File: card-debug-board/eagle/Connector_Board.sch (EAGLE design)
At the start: 26 parts, among them J1 ORESAT-DEBUG-CONNECTOR-CARD, J3 USB_A_SMT_FEMALE, U1 FT230XS-R

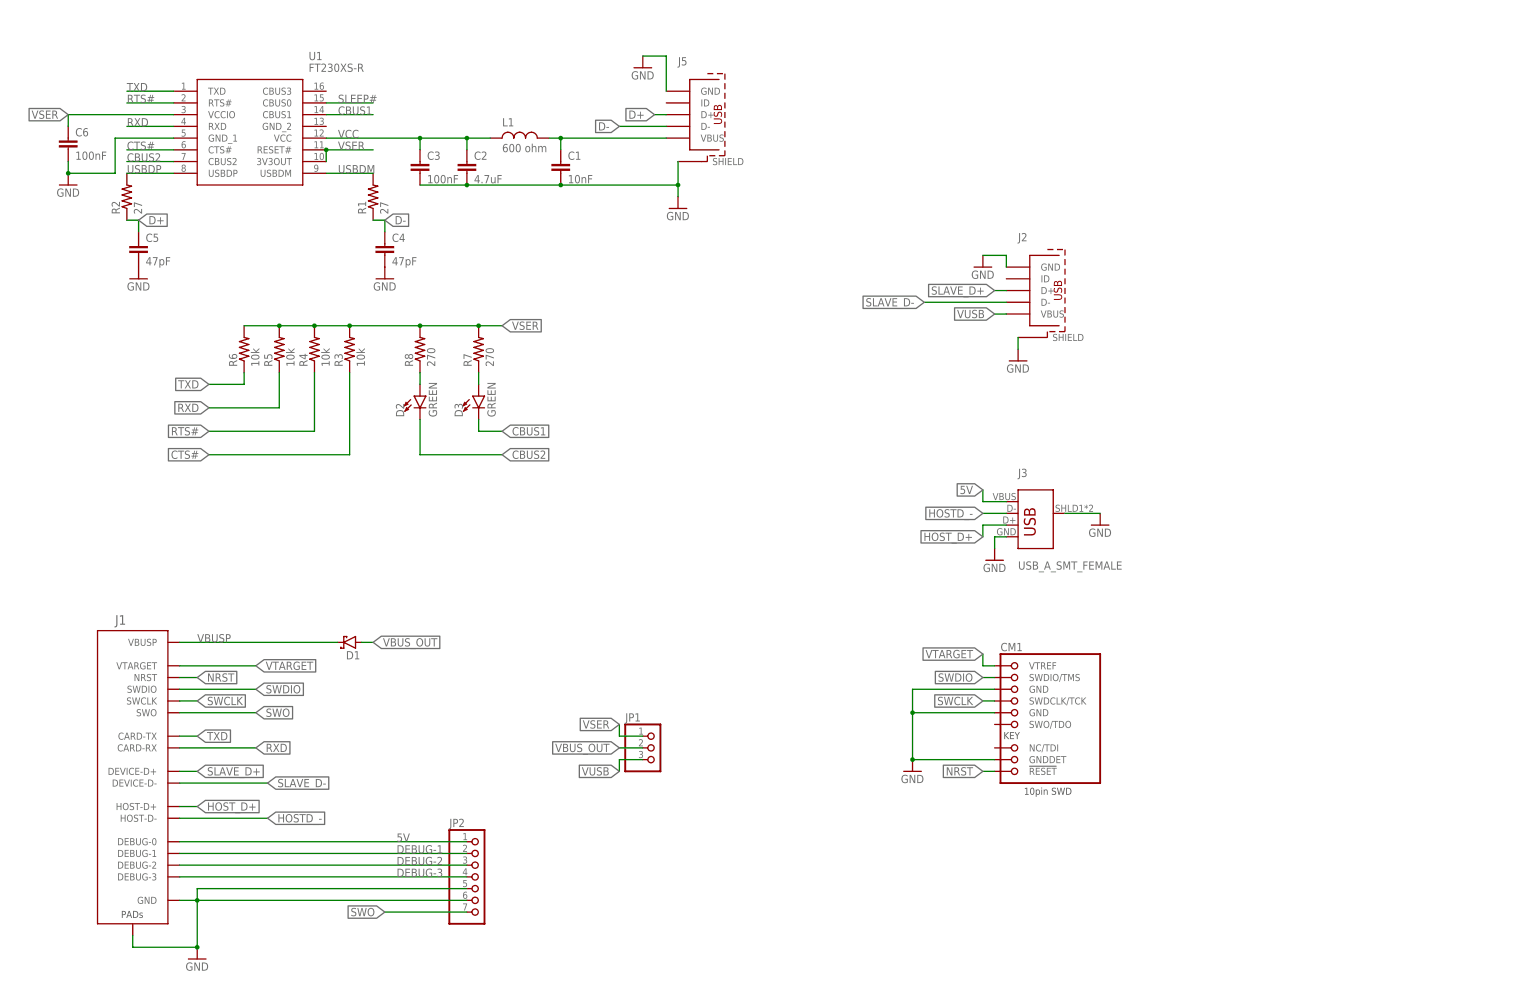
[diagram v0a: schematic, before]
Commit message: Added lables, diff pairs , GND vias
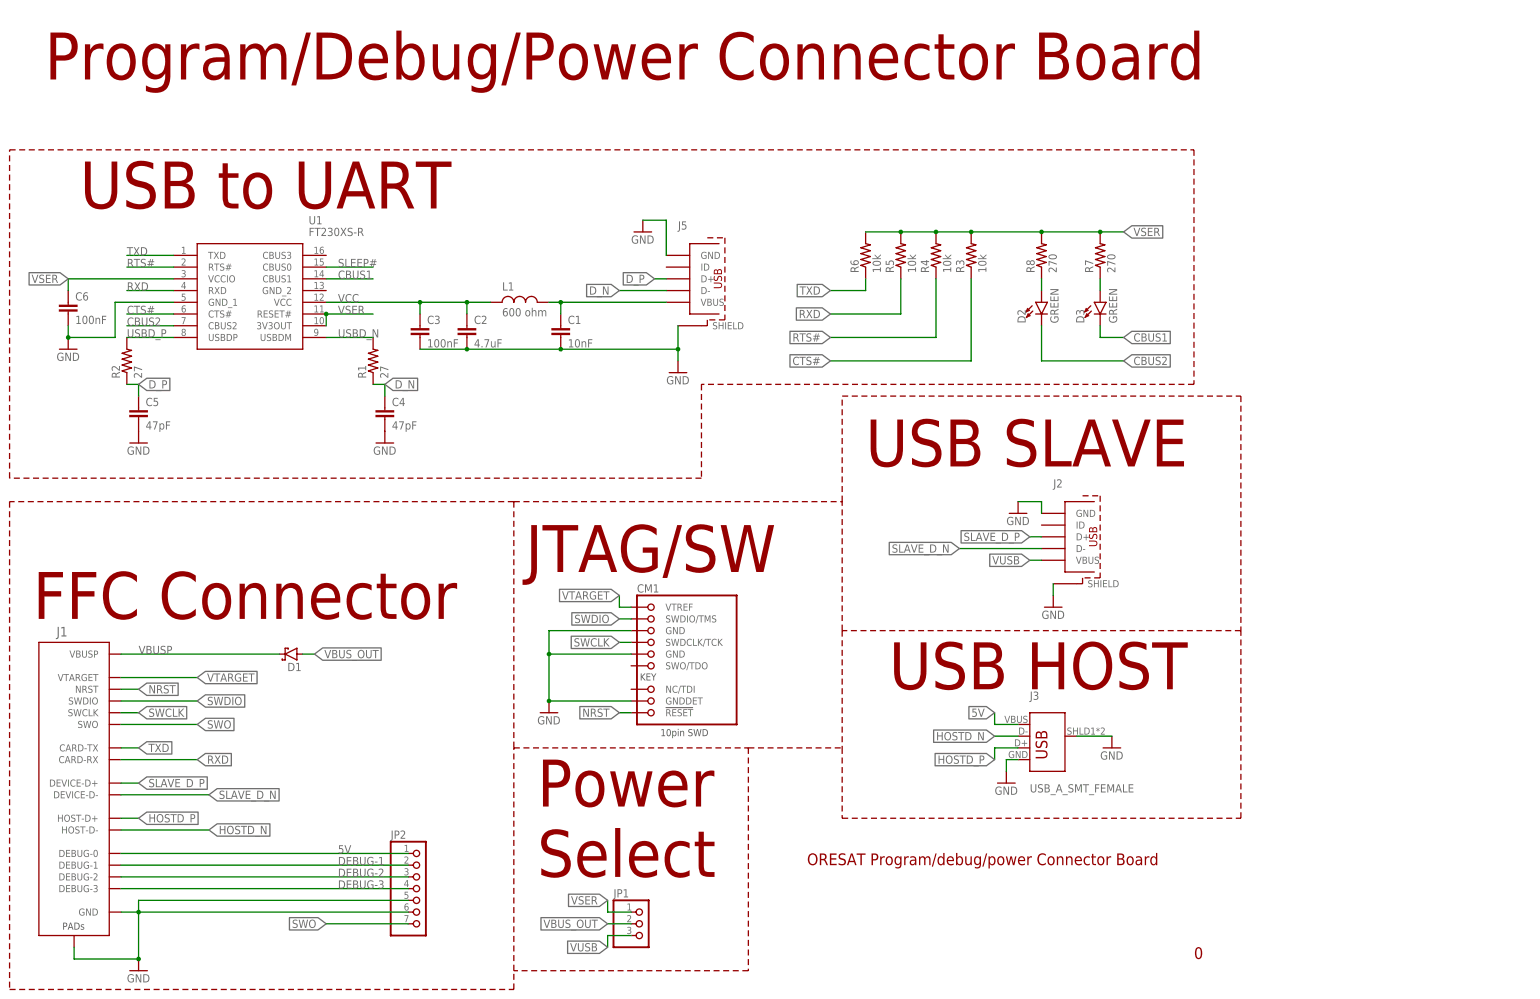
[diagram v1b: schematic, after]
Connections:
- net D+ renamed D_P
- net D- renamed D_N
- net HOSTD_- renamed HOSTD_N
- net HOST_D+ renamed HOSTD_P
- net SLAVE_D+ renamed SLAVE_D_P
- net SLAVE_D- renamed SLAVE_D_N
- net USBDM renamed USBD_N
- net USBDP renamed USBD_P
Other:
- note added: "0"
- note added: "FFC Connector"
- note added: "JTAG/SW"
- note added: "ORESAT Program/debug/power Connector Board"
- note added: "Power Select"
- note added: "Program/Debug/Power Connector Board"
- note added: "USB HOST"
- note added: "USB SLAVE"
- note added: "USB to UART"
- moved on the sheet: C1, C2, C3, C4, C5, C6, CM1, D1, D2, D3, J1, J2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

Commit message: Added P Channel  MOSFET switched VUSB
Made Voltage buses wider
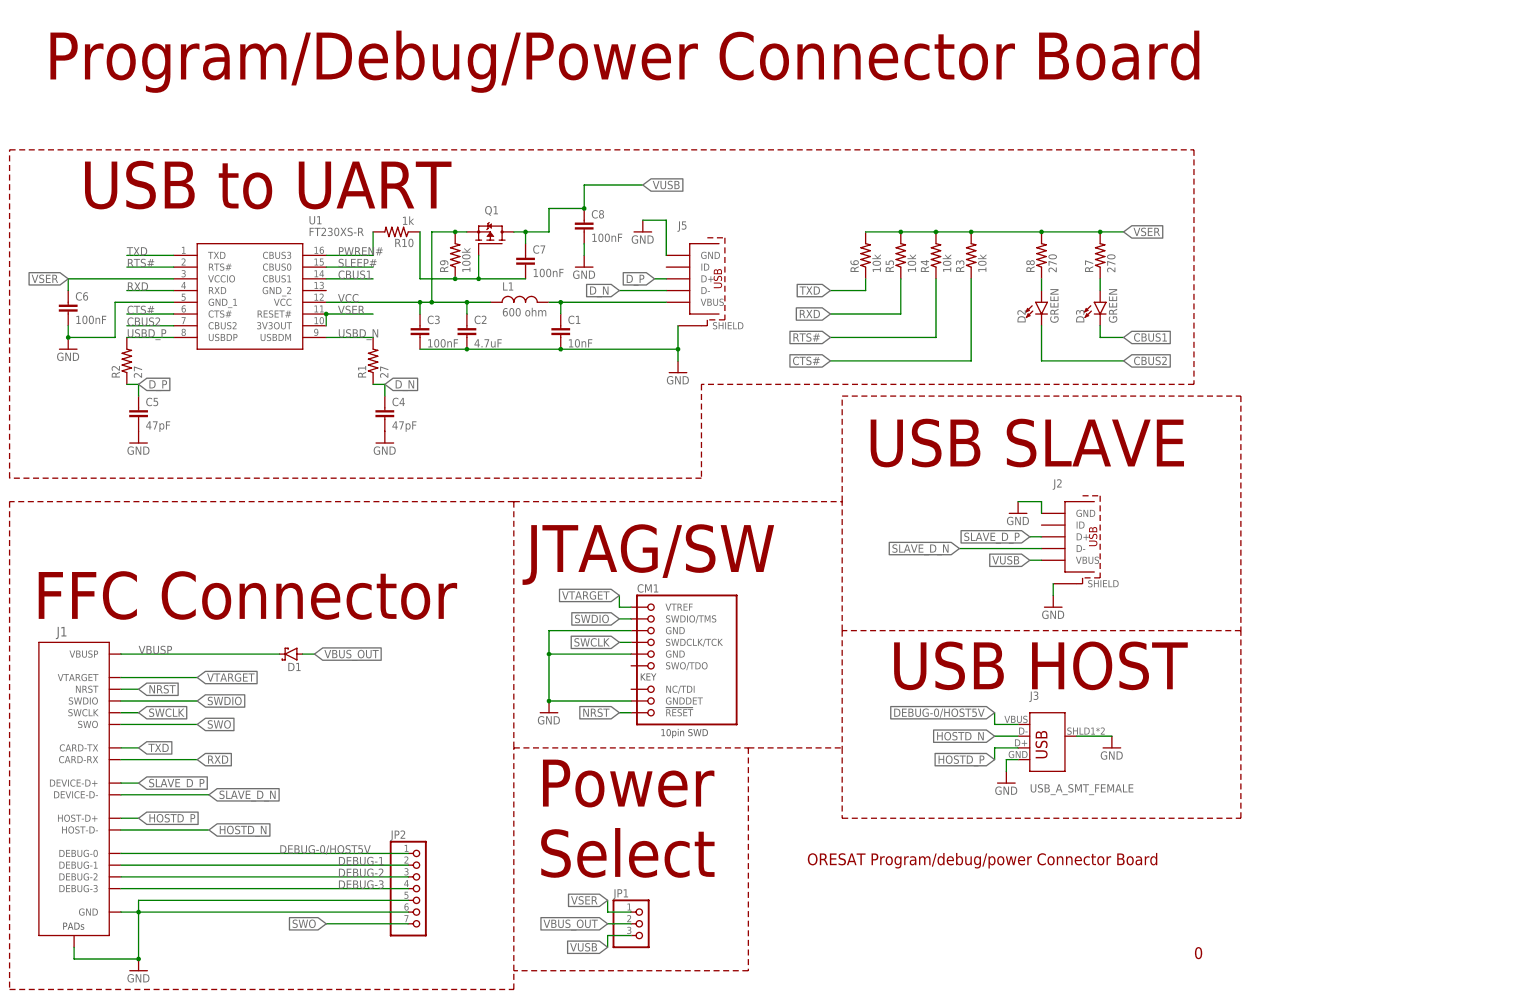
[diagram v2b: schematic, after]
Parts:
- added C7, C8: 100nF, oresat-rcl:C-EU0603-C-NOSILK
- added Q1: MOSFET-PCH-SOT23-6, Q-MOSFET-PCH-SOT23-6:MOSFET-PCH-SOT23-6
- added R10: 1k, oresat-rcl:R-US_0603-C-NOSILK
- added R9: 100k, oresat-rcl:R-US_0603-C-NOSILK
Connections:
- net 5V renamed DEBUG-0/HOST5V
- new net N$3: C7.2, Q1.G, R10.1, R9.1
- new net PWREN#: R10.2, U1.CBUS3
- net GND: now also C8.2
- net VCC: now also Q1.S, R9.2
- net VUSB: now also C7.1, C8.1, Q1.D
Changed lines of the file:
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@@
 <part name="D2" library="SparkFun-LED" library_urn="urn:adsk.eagle:library:529" deviceset="LED-GREEN" device="0603" package3d_urn="urn:adsk.eagle:package:39354/1" value="GREEN"/>
 <part name="D3" library="SparkFun-LED" library_urn="urn:adsk.eagle:library:529" deviceset="LED-GREEN" device="0603" package3d_urn="urn:adsk.eagle:package:39354/1" value="GREEN"/>
+<part name="Q1" library="Q-MOSFET-PCH-SOT23-6" deviceset="MOSFET-PCH-SOT23-6" device=""/>
+<part name="R9" library="oresat-rcl" deviceset="R-US_" device="0603-C-NOSILK" value="100k"/>
+<part name="R10" library="oresat-rcl" deviceset="R-US_" device="0603-C-NOSILK" value="1k"/>
+<part name="C7" library="oresat-rcl" deviceset="C-EU" device="0603-C-NOSILK" value="100nF"/>
+<part name="C8" library="oresat-rcl" deviceset="C-EU" device="0603-C-NOSILK" value="100nF"/>
+<part name="GND12" library="supply1" library_urn="urn:adsk.eagle:library:371" deviceset="GND" device=""/>
 </parts>
 <sheets>
@@
 <attribute name="VALUE" x="245.745" y="145.288" size="1.778" layer="96" font="vector" rot="R90" align="top-left"/>
 </instance>
+<instance part="Q1" gate="G$1" x="111.76" y="162.56" smashed="yes" rot="R90">
+<attribute name="NAME" x="110.49" y="168.91" size="1.778" layer="95"/>
+</instance>
+<instance part="R9" gate="R" x="104.14" y="160.02" smashed="yes" rot="R90">
+<attribute name="NAME" x="102.6414" y="156.21" size="1.778" layer="95" rot="R90"/>
+<attribute name="VALUE" x="107.442" y="156.21" size="1.778" layer="96" rot="R90"/>
+</instance>
+<instance part="R10" gate="R" x="91.44" y="165.1" smashed="yes" rot="R180">
+<attribute name="NAME" x="95.25" y="163.6014" size="1.778" layer="95" rot="R180"/>
+<attribute name="VALUE" x="95.25" y="168.402" size="1.778" layer="96" rot="R180"/>
+</instance>
+<instance part="C7" gate="CE" x="119.38" y="160.02" smashed="yes">
+<attribute name="NAME" x="120.904" y="160.401" size="1.778" layer="95"/>
+<attribute name="VALUE" x="120.904" y="155.321" size="1.778" layer="96"/>
+</instance>
+<instance part="C8" gate="CE" x="132.08" y="167.64" smashed="yes">
+<attribute name="NAME" x="133.604" y="168.021" size="1.778" layer="95"/>
+<attribute name="VALUE" x="133.604" y="162.941" size="1.778" layer="96"/>
+</instance>
+<instance part="GND12" gate="1" x="132.08" y="157.48" smashed="yes">
+<attribute name="VALUE" x="129.54" y="154.94" size="1.778" layer="96"/>
+</instance>
 </instances>
 <busses>
@@
 <wire x1="30.48" y1="142.24" x2="20.32" y2="142.24" width="0.1524" layer="91"/>
 </segment>
+<segment>
+<pinref part="C8" gate="CE" pin="2"/>
+<pinref part="GND12" gate="1" pin="GND"/>
+<wire x1="132.08" y1="162.56" x2="132.08" y2="160.02" width="0.1524" layer="91"/>
+</segment>
 </net>
 <net name="VUSB" class="0">
@@
 <label x="228.6" y="93.98" size="1.778" layer="95" rot="R180" xref="yes"/>
 </segment>
+<segment>
+<pinref part="Q1" gate="G$1" pin="D"/>
+<pinref part="C7" gate="CE" pin="1"/>
+<pinref part="C8" gate="CE" pin="1"/>
+<wire x1="124.46" y1="165.1" x2="124.46" y2="170.18" width="0.1524" layer="91"/>
+<wire x1="124.46" y1="170.18" x2="132.08" y2="170.18" width="0.1524" layer="91"/>
+<wire x1="116.84" y1="165.1" x2="119.38" y2="165.1" width="0.1524" layer="91"/>
+<wire x1="119.38" y1="165.1" x2="119.38" y2="162.56" width="0.1524" layer="91"/>
+<wire x1="119.38" y1="165.1" x2="124.46" y2="165.1" width="0.1524" layer="91"/>
+<junction x="119.38" y="165.1"/>
+<wire x1="132.08" y1="170.18" x2="132.08" y2="175.26" width="0.1524" layer="91"/>
+<wire x1="132.08" y1="175.26" x2="144.78" y2="175.26" width="0.1524" layer="91"/>
+<junction x="132.08" y="170.18"/>
+<label x="144.78" y="175.26" size="1.778" layer="95" xref="yes"/>
+</segment>
 </net>
 <net name="VBUS_OUT" class="0">
@@
 </segment>
 </net>
-<net name="5V" class="0">
+<net name="DEBUG-0/HOST5V" class="0">
 <segment>
 <pinref part="JP2" gate="A" pin="1"/>
 <pinref part="J1" gate="G$1" pin="DEBUG-0"/>
 <wire x1="31.75" y1="30.48" x2="93.98" y2="30.48" width="0.1524" layer="91"/>
-<label x="78.74" y="30.48" size="1.778" layer="95"/>
+<label x="66.04" y="30.48" size="1.778" layer="95"/>
 </segment>
 <segment>
@@
 <wire x1="111.76" y1="149.86" x2="106.68" y2="149.86" width="0.1524" layer="91"/>
 <pinref part="C3" gate="CE" pin="1"/>
-<wire x1="106.68" y1="149.86" x2="96.52" y2="149.86" width="0.1524" layer="91"/>
+<wire x1="106.68" y1="149.86" x2="99.06" y2="149.86" width="0.1524" layer="91"/>
+<wire x1="99.06" y1="149.86" x2="96.52" y2="149.86" width="0.1524" layer="91"/>
 <wire x1="96.52" y1="149.86" x2="76.2" y2="149.86" width="0.1524" layer="91"/>
 <wire x1="96.52" y1="149.86" x2="96.52" y2="147.32" width="0.1524" layer="91"/>
@@
 <junction x="106.68" y="149.86"/>
 <label x="78.74" y="149.86" size="1.778" layer="95"/>
+<pinref part="R9" gate="R" pin="2"/>
+<pinref part="Q1" gate="G$1" pin="S"/>
+<wire x1="104.14" y1="165.1" x2="106.68" y2="165.1" width="0.1524" layer="91"/>
+<wire x1="104.14" y1="165.1" x2="99.06" y2="165.1" width="0.1524" layer="91"/>
+<wire x1="99.06" y1="165.1" x2="99.06" y2="149.86" width="0.1524" layer="91"/>
+<junction x="104.14" y="165.1"/>
+<junction x="99.06" y="149.86"/>
 </segment>
 </net>
@@
 </segment>
 </net>
+<net name="PWREN#" class="0">
+<segment>
+<pinref part="U1" gate="G$1" pin="CBUS3"/>
+<pinref part="R10" gate="R" pin="2"/>
+<wire x1="86.36" y1="165.1" x2="86.36" y2="160.02" width="0.1524" layer="91"/>
+<wire x1="86.36" y1="160.02" x2="76.2" y2="160.02" width="0.1524" layer="91"/>
+<label x="78.74" y="160.02" size="1.778" layer="95"/>
+</segment>
+</net>
+<net name="N$3" class="0">
+<segment>
+<pinref part="Q1" gate="G$1" pin="G"/>
+<wire x1="109.22" y1="160.02" x2="109.22" y2="154.94" width="0.1524" layer="91"/>
+<pinref part="R9" gate="R" pin="1"/>
+<wire x1="109.22" y1="154.94" x2="104.14" y2="154.94" width="0.1524" layer="91"/>
+<pinref part="C7" gate="CE" pin="2"/>
+<wire x1="119.38" y1="154.94" x2="109.22" y2="154.94" width="0.1524" layer="91"/>
+<junction x="109.22" y="154.94"/>
+<pinref part="R10" gate="R" pin="1"/>
+<wire x1="96.52" y1="165.1" x2="96.52" y2="154.94" width="0.1524" layer="91"/>
+<wire x1="96.52" y1="154.94" x2="104.14" y2="154.94" width="0.1524" layer="91"/>
+<junction x="104.14" y="154.94"/>
+</segment>
+</net>

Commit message: Added jumper select for Host5V or Debug-0
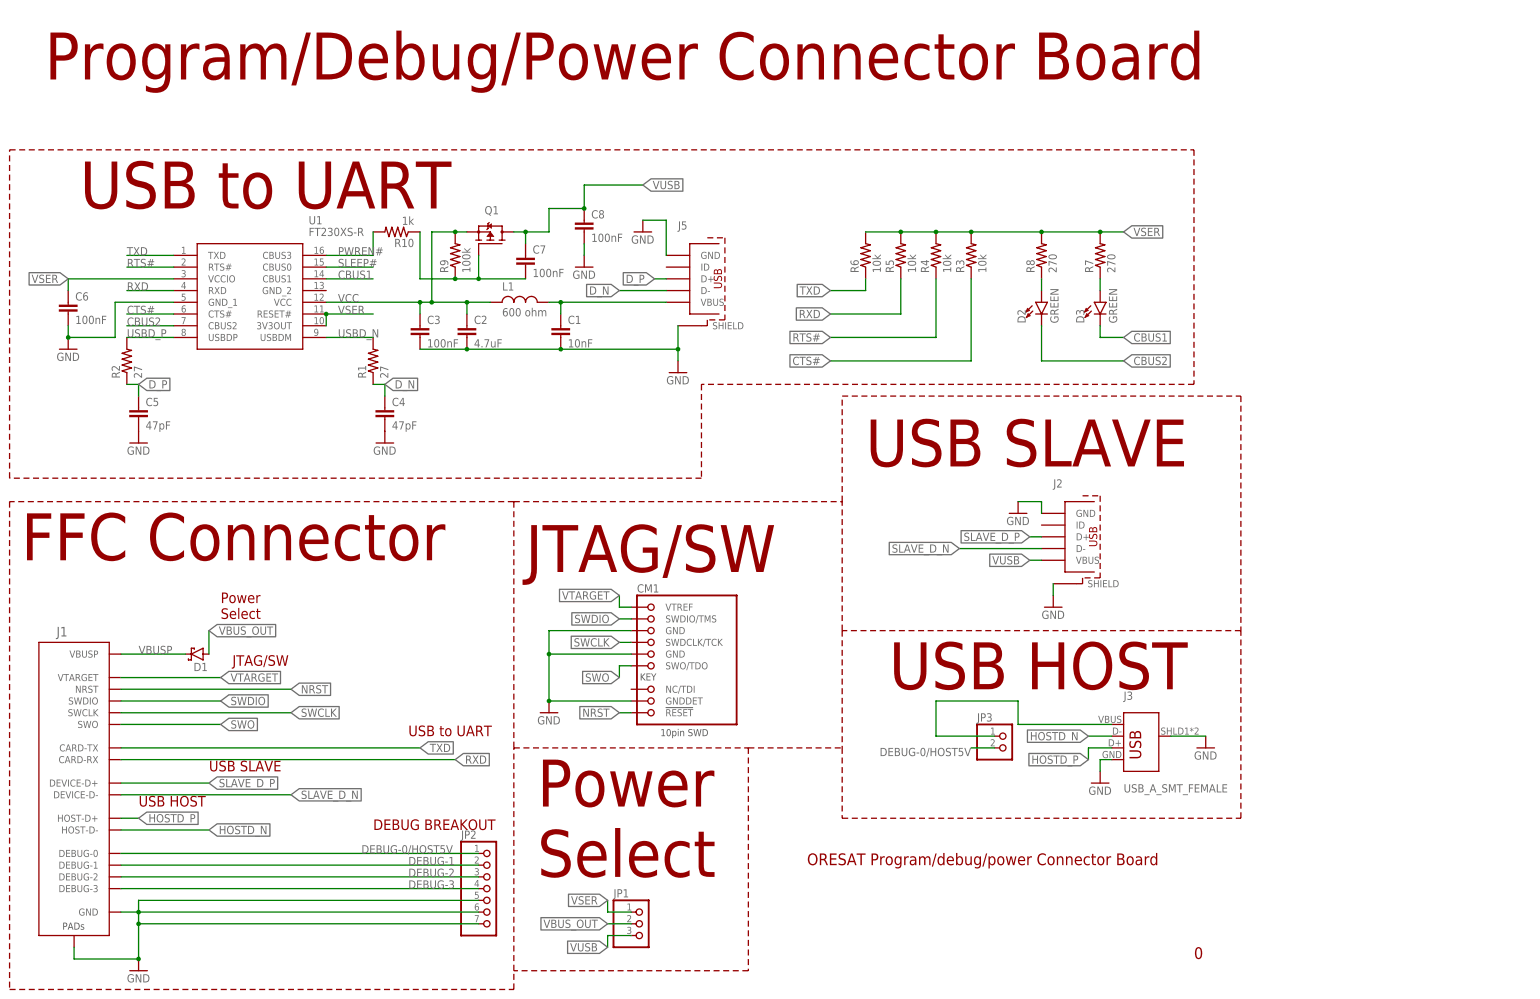
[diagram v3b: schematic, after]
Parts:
- added JP3: (no value), pinhead:PINHD-1X2
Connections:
- new net N$2: J3.VBUS, JP3.1
- net DEBUG-0/HOST5V: now also JP3.2; no longer J3.VBUS
- net GND: now also JP2.7
- net SWO: now also CM1.SWO/TDO; no longer JP2.7
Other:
- note added: "DEBUG BREAKOUT"
- moved on the sheet: D1, J3, JP2
